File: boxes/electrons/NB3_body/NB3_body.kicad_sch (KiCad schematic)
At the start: 34 parts, among them J1 Conn_02x05_Counter_Clockwise, J10 Conn_02x03_Top_Bottom, J11 Conn_02x03_Top_Bottom, J12 Conn_02x03_Top_Bottom, J13 JST ZH 6-way Socket, J14 JST ZH 6-way Socket, J2 Conn_02x05_Counter_Clockwise, J3 Conn_02x05_Counter_Clockwise, J4 Conn_02x05_Counter_Clockwise, J5 Conn_02x05_Counter_Clockwise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

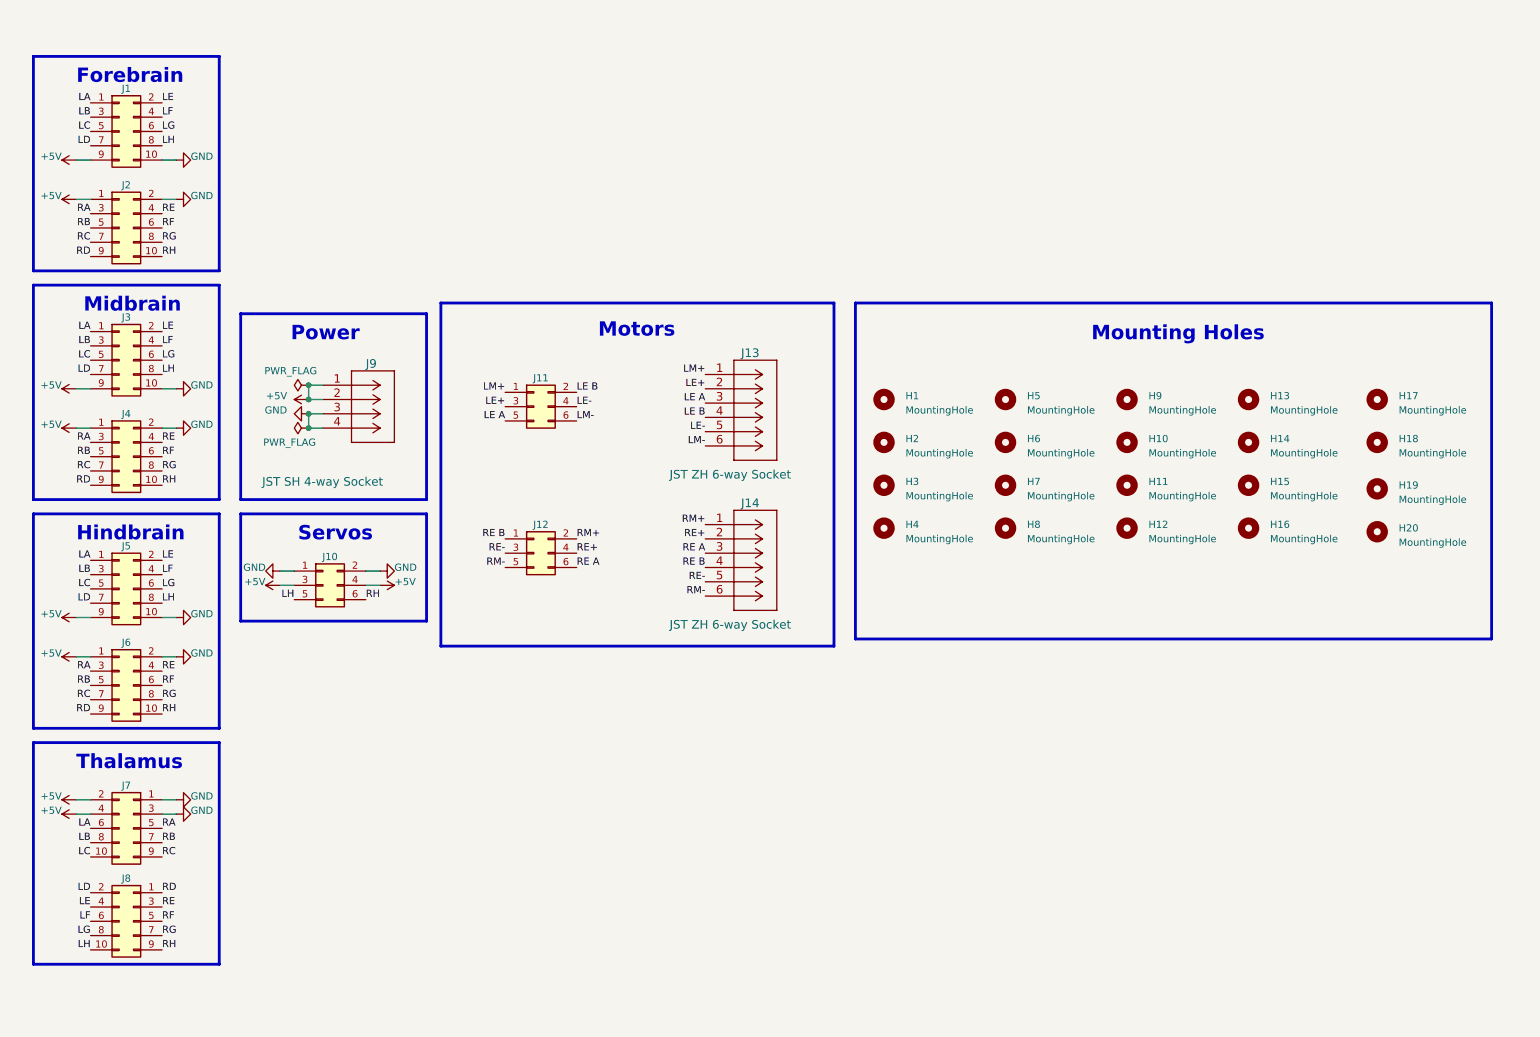
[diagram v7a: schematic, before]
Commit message: Update NB3 Body (for servo drive)
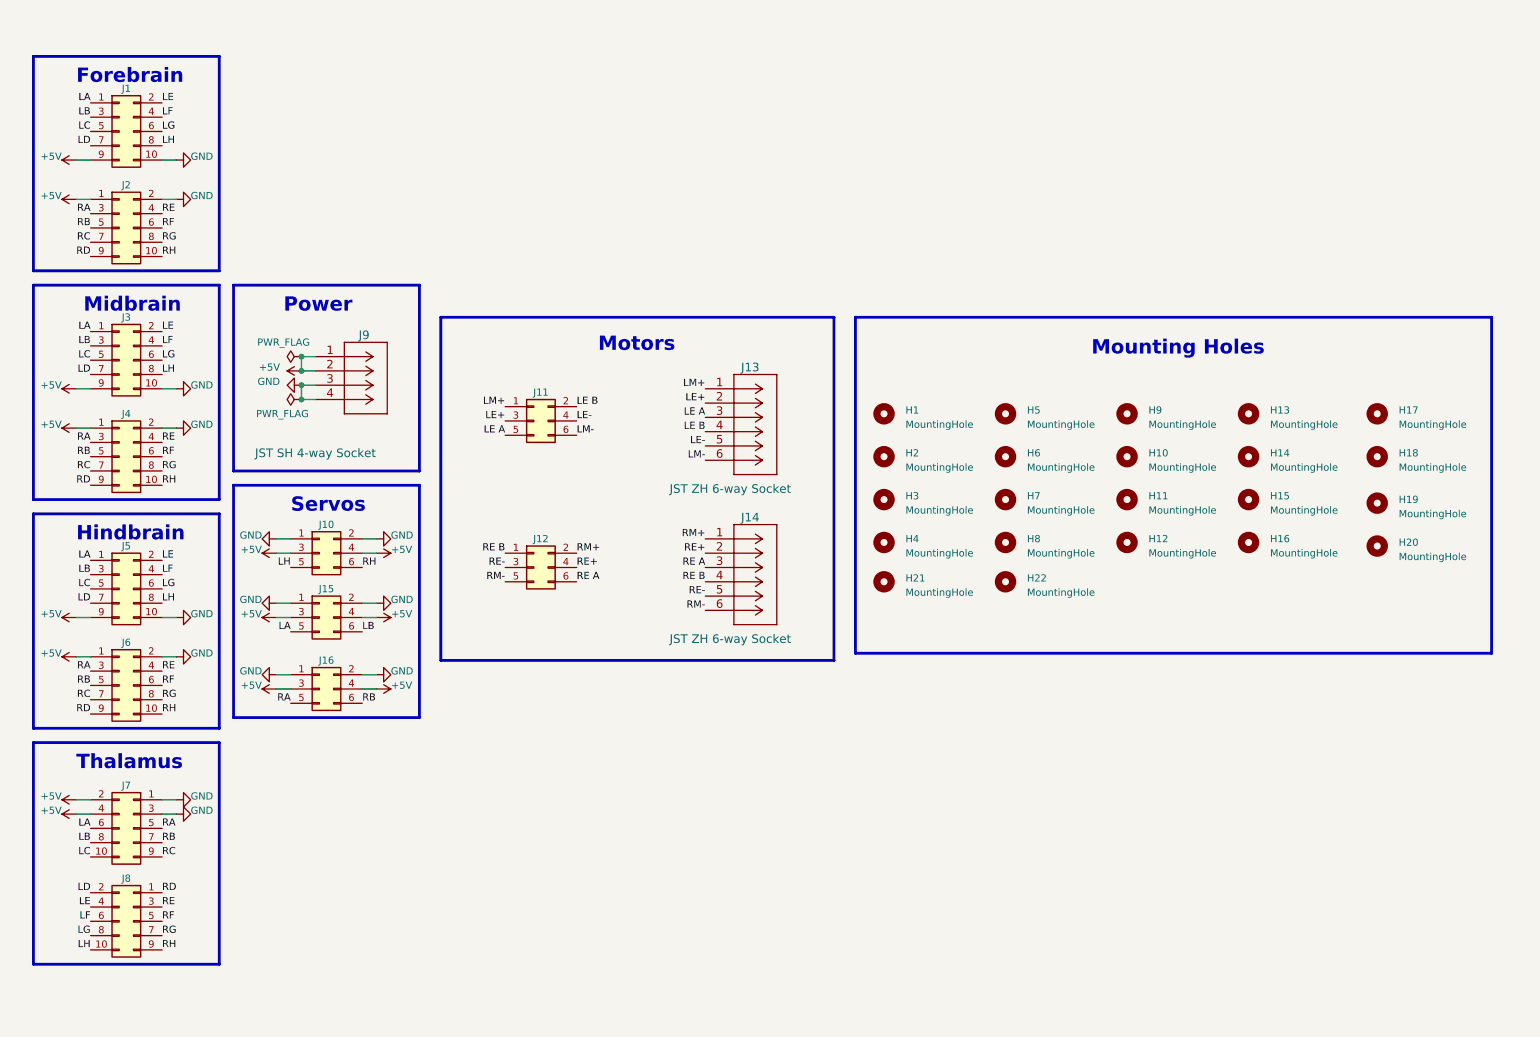
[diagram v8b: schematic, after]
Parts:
- added H21, H22: MountingHole, MountingHole:MountingHole_2.5mm_Pad, symbol Mechanical:MountingHole
- added J15, J16: Conn_02x03_Top_Bottom, Connector_PinHeader_2.54mm:PinHeader_2x03_P2.54mm_Vertical_SMD, symbol Connector_Generic:Conn_02x03_Odd_Even
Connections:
- net +5V: now also J15.3 (Pin_3), J15.4 (Pin_4), J16.3 (Pin_3), J16.4 (Pin_4)
- net GND: now also J15.1 (Pin_1), J15.2 (Pin_2), J16.1 (Pin_1), J16.2 (Pin_2)
- net LA: now also J15.5 (Pin_5)
- net LB: now also J15.6 (Pin_6)
- net RA: now also J16.5 (Pin_5)
- net RB: now also J16.6 (Pin_6)
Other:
- moved on the sheet: H1, H10, H11, H12, H13, H14, H15, H16, H17, H18, H19, H2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
